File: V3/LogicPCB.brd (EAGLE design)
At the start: 171.9 x 151.6 mm, 58 parts, among them CON1 CUBE_ORANGE_, CON13 CON-6P-JST-XA, CON14 PINHEAD_1X04-2.54, CON15 CON-4P-JST-XA, CON17 CON-4P-JST-XA, CON18 CON-6P-JST-XA, CON19 USB-TYPE-C-VERT-PROD, CON2 CON-4P-JST-XA, CON20 PINHEAD_1X06-2.54, CON21 CON-4P-JST-XA, CON22 CON-4P-JST-XA, CON23 CON-4P-JST-XA, CON24 CON-4P-JST-XA, CON25 CON-4P-JST-XA, CON26 CON-4P-JST-XA, CON27 CON-4P-JST-XA, CON28 CON-4P-JST-XA, CON29 CON-4P-JST-XA, CON3 PINHEAD_1X08-2.54, CON30 CON-4P-JST-XA, CON32 CON-4P-JST-XA, CON35 CON-12P-JST-XA, CON4 CON-2P-JST-XA, CON5 CON-6P-JST-XA, CON6 CON-4P-JST-XA, CON7 PINHEAD_1X06-2.54, CON8 PINHEAD_1X08-2.54, IC2 AOZ1280, M1 05G_ETHERNET_SWITCH, Q1 IRLML0030

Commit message: updates for V3
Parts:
- removed CON3: PINHEAD_1X08-2.54, pinhead:1X08-PTH-2.54
- added CON9: PINHEAD_1X12-2.54, pinhead:1X12-PTH-2.54
- moved R2 3.47 mm to (-45.9, 56.5)
- moved SJ2 3.47 mm to (-48.2, 56.1)
- moved D10 3.16 mm to (-3.72, 53.8)
- moved R38 3.16 mm to (-7.10, 54.7)
- moved R37 3.16 mm to (-6.20, 56.3)
- moved CON30 2.24 mm to (26.4, 25.2)
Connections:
- net CAM_RX+ renamed ETH3_TX+
- net CAM_TX+ renamed ETH3_RX+
- net CAM_TX- renamed ETH3_RX-
- net CAN_RX- renamed ETH3_TX-
- net N$10 renamed ETH1_TX+
- net N$11 renamed ETH1_TX-
- net N$12 renamed ETH1_RX+
- net N$17 renamed ETH1_RX-
- net PL_ETH_RX+ renamed ETH5_TX-
- net PL_ETH_RX- renamed ETH5_TX+
- net PL_ETH_TX+ renamed ETH5_RX-
- net PL_ETH_TX- renamed ETH5_RX+
- net 5VFMU: now also CON9.6, CON9.7, CON9.8; no longer CON3.6, CON3.7, CON3.8
- net BATT_CURRENT: now also CON9.1; no longer CON3.1
- net BATT_VOLTAGE: now also CON9.2; no longer CON3.2
- net GND: now also CON35.10, CON9.11, CON9.12, CON9.3, CON9.4, CON9.5; no longer CON3.3, CON3.4, CON3.5
- net SERIAL3_RX: now also CON35.6; no longer CON35.8
- net SERIAL3_TX: now also CON35.5; no longer CON35.7
- net VDD_24V: now also CON35.7, CON35.8; no longer CON35.10
- net VDD_4V: now also CON9.10, CON9.9
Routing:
- net VDD_4V: track 31.3 -> 75.2 mm
- net CAN1_H: track 560.4 -> 547.7 mm
- net CAN1_L: track 565.9 -> 554.3 mm
- net M3PWM: track 83.7 -> 94.3 mm
- net M2PWM: track 88.3 -> 84.9 mm
- net N$23: track 9.40 -> 12.6 mm
- net SERIAL2_TX: track 47.5 -> 44.7 mm
- net SERIAL2_RX: track 45.2 -> 42.4 mm
- net 5VFMU: track 78.0 -> 75.2 mm
- net N$22: track 9.56 -> 12.3 mm
- net ETH3_TX+: track 94.2 -> 96.3 mm
- net ETH3_RX+: track 93.3 -> 95.4 mm
- net ETH3_TX-: track 93.5 -> 95.6 mm
- net ETH3_RX-: track 94.5 -> 96.6 mm
- net VDD_24V: track 57.6 -> 59.1 mm
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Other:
- board text added: "+"
- board text added: "CAN1 TERMINATION"
- board text added: "CTS"
- board text added: "CTS_4"
- board text added: "RX_4"
- board text added: "SER_RX"
- board text added: "SER_TX"
- board text added: "TX_4"
- board text removed: "ALT"
- board text removed: "B1H"
- board text removed: "B1L"
- board text removed: "B2H"
- board text removed: "B2L"
- board text removed: "B3H"
- board text removed: "B3L"
- board text removed: "BEACON"
- board text removed: "BTN"
- board text removed: "CAM"
- board text removed: "CAN1"
- board text removed: "CAN2"
- board text removed: "CR123A battery"
- board text removed: "DATA"
- board text removed: "DATA LINK"
- board text removed: "I2C"
- board text removed: "M1"
- board text removed: "M2"
- board text removed: "M4"
- board text removed: "M5"
- board text removed: "M6"
- board text removed: "PAYLOAD"
- board text removed: "PWRBTN"
- board text removed: "RES1"
- board text removed: "RX1"
- board text removed: "RX2"
- board text removed: "TELEM SBUS"
- board text removed: "TX1"
- board text removed: "TX2"

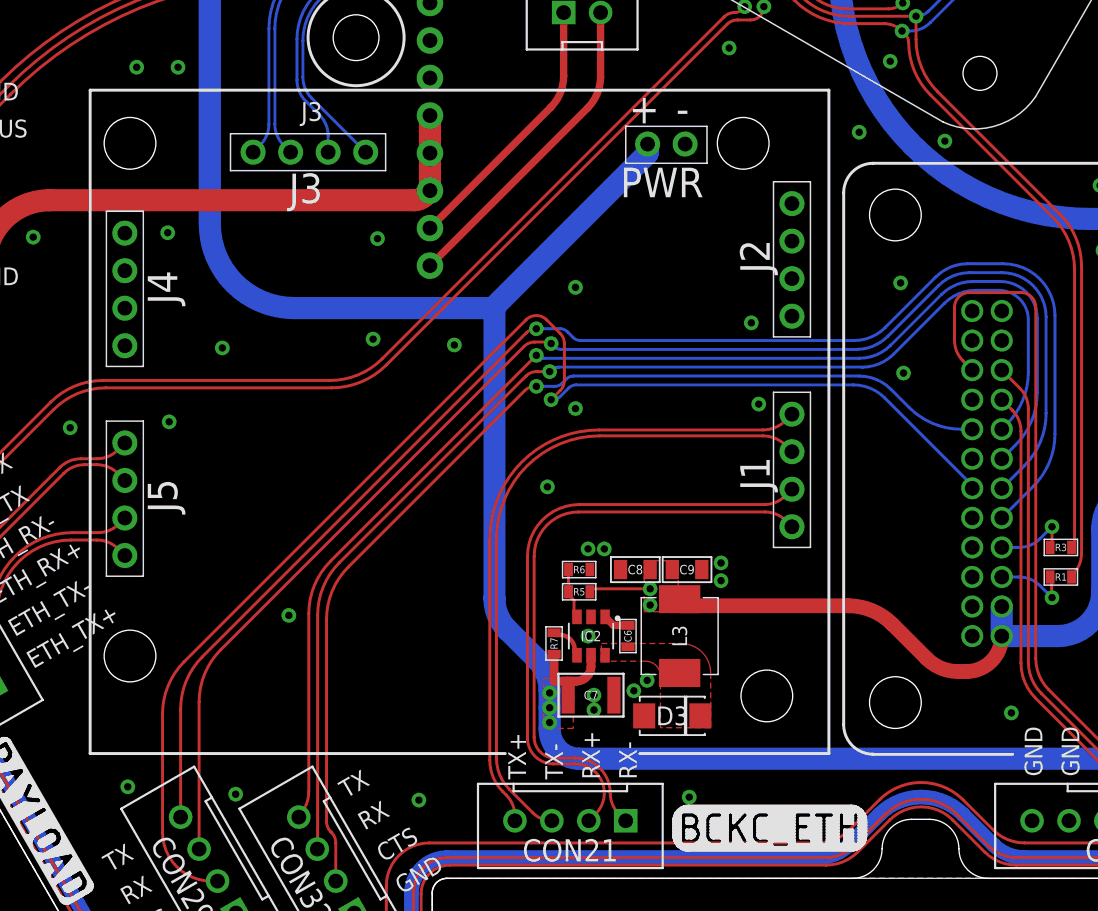
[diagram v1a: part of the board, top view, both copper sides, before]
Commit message: silkscreen updates
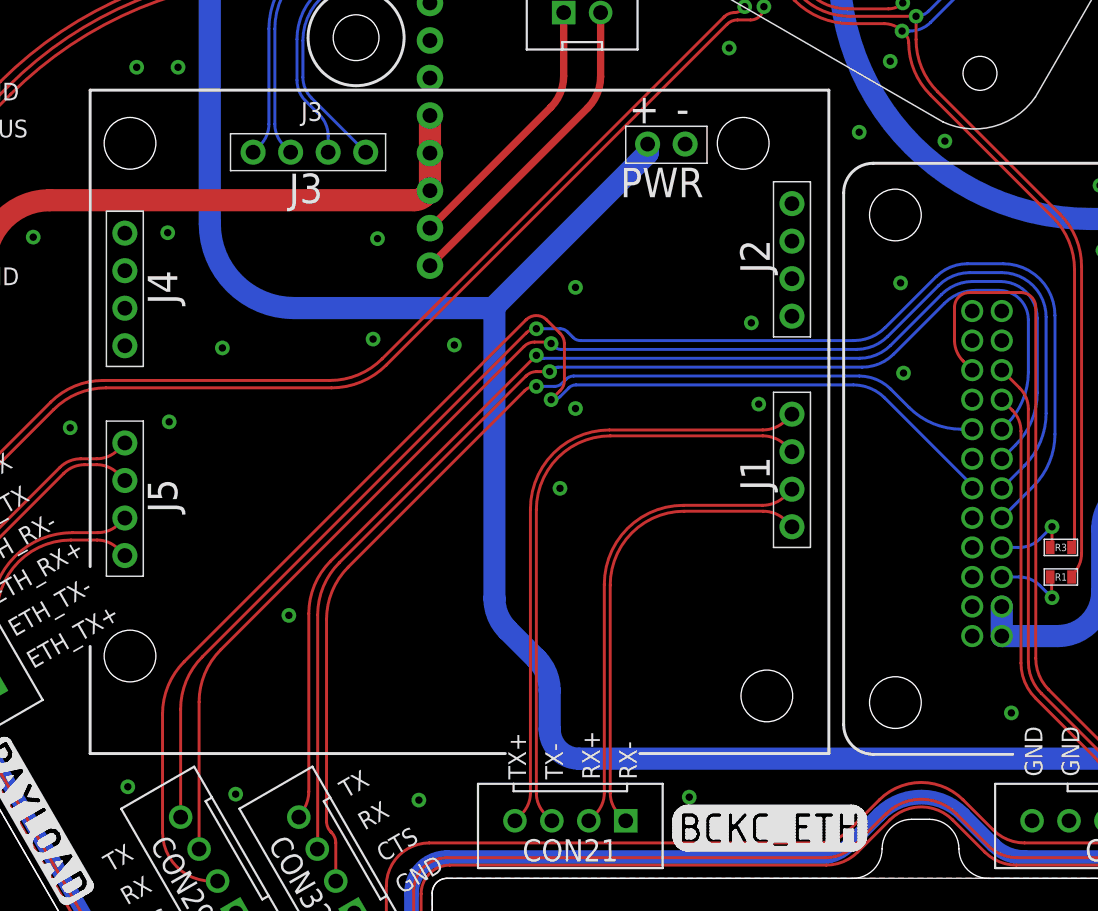
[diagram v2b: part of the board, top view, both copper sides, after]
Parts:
- removed C6: 22nF, rc:C0603
- removed C7: 10uF, rc:C1210
- removed C8, C9: 22uF, rc:C0805
- removed D3: SS34, Diodes:DO-214AC(SMA)
- removed IC2: AOZ1280, dc-dc:SOT23-6
- removed L3: 3.3uH, power_inductors:IHLP-2020BZ-01
- removed R5, R6: ???, rc:R0603
- removed R7: 51K, rc:R0603
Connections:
- removed net N$14: C6.2, IC2.1
- removed net N$15: IC2.3, R5.1, R6.1
- removed net N$16: IC2.4, R7.1
- removed net SW2: C6.1, D3.C, IC2.6, L3.P$1
- net GND: no longer C7.1, C8.1, C9.1, D3.A, IC2.2, R6.2
- net VDD_12V: no longer C7.2, IC2.5, R7.2
- net VDD_4V: no longer C8.2, C9.2, L3.P$2, R5.2
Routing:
- net VDD_4V: track 75.2 -> 45.9 mm, vias 2 -> 0
- net ETH1_RX+: track 40.9 -> 31.5 mm
- net ETH1_RX-: track 40.1 -> 30.9 mm
- net VDD_12V: track 270.8 -> 264.1 mm, vias 3 -> 0
- net N$15: track 3.44 -> 0.00 mm
- net ETH1_TX-: track 43.9 -> 41.0 mm
- net N$16: track 2.34 -> 0.00 mm
- net N$14: track 1.79 -> 0.00 mm
- net ETH1_TX+: track 43.3 -> 41.6 mm
- net GND: vias 113 -> 104
- removed copper zone on layer 1, net SW2
- removed copper zone on layer 1, net VDD_12V
- removed copper zone on layer 1, net VDD_4V

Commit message: V3 finalization
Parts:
- added C4: 10u, rc:C1206
- added C56: 10n, rc:C0603
- added C8: 47u, rc:C1206
- added CON11: CON-4P-JST-XA, Connectors:B04B-XASK-1
- added CON3: PINHEAD_1X04-2.54, pinhead:1X04-PTH-2.54
- added D11: SS34, Diodes:DO-214AC(SMA)
- added IC5: AOZ1280, dc-dc:SOT23-6
- added L1: 3.3uH, power_inductors:IHLP-2020BZ-01
- added M2: 05G_ETHERNET_SWITCH, ali_modules:05G_ETH_SWITCH
- added MODULE2: HLK-7688A, ali_modules:HLK-7688A
- added R30, R32: 51K, rc:R0603
- added R31: 16K, rc:R0603
- added T1, T2, T3, T4: H1102NL, misc:H1102
- moved R22 0.67 mm to (26.3, 52.7)
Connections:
- new net CAM_RX+: T1.9
- new net CAM_TX+: T1.14
- new net CAM_TX-: T1.16
- new net CAN_RX-: T1.11
- new net HLK_RX0: MODULE2.32
- new net HLK_RX1: MODULE2.16
- new net HLK_TX0: MODULE2.31
- new net HLK_TX1: MODULE2.15
- new net LINK0: MODULE2.13
- new net LINK1: MODULE2.12
- new net LINK2: MODULE2.11
- new net LINK4: MODULE2.9
- new net LINK_RX+: T4.9
- new net LINK_RX-: T4.11
- new net LINK_TX+: T4.14
- new net LINK_TX-: T4.16
- new net N$88: C56.2, IC5.1
- new net N$90: IC5.3, R30.1, R31.1
- new net N$91: IC5.4, R32.1
- new net P0_RX+: MODULE2.34, T2.3
- new net P0_RX-: MODULE2.35, T2.1
- new net P0_TX+: MODULE2.36, T2.8
- new net P0_TX-: MODULE2.37, T2.6
- new net P1_RX+: MODULE2.40, T1.8
- new net P1_RX-: MODULE2.41, T1.6
- new net P1_TX+: MODULE2.38, T1.3
- new net P1_TX-: MODULE2.39, T1.1
- new net P2_RX+: MODULE2.42, T4.8
- new net P2_RX-: MODULE2.43, T4.6
- new net P2_TX+: MODULE2.44, T4.3
- new net P2_TX-: MODULE2.45, T4.1
- new net P4_RX+: MODULE2.50, T3.8
- new net P4_RX-: MODULE2.51, T3.6
- new net P4_TX+: MODULE2.52, T3.3
- new net P4_TX-: MODULE2.53, T3.1
- new net PL_ETH_RX+: T3.11
- new net PL_ETH_RX-: T3.9
- new net PL_ETH_TX+: T3.16
- new net PL_ETH_TX-: T3.14
- new net SW: C56.1, D11.C, IC5.6, L1.P$1
- new net USB_DM: CON3.4, MODULE2.55
- new net USB_DP: CON3.3, MODULE2.54
- new net VDD_3V3: C8.P$1, L1.P$2, MODULE2.2, MODULE2.3, R30.2
- net GND: now also C4.P$1, C8.P$2, CON11.1, CON3.1, D11.A, IC5.2, MODULE2.1, MODULE2.21, MODULE2.23, MODULE2.4, MODULE2.56, MODULE2.P$1, MODULE2.P$2, MODULE2.P$3, R31.2
- net SERIAL4_RX: now also CON11.4; no longer CON30.4
- net SERIAL4_TX: now also CON11.3; no longer CON30.3
- net SERIAL5_RX: now also CON30.4
- net SERIAL5_TX: now also CON30.3
- net VDD_12V: now also C4.P$2, CON3.2, IC5.5, R32.2
- net VDD_5V: now also CON11.2
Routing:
- net SERIAL5_RX: track 0.00 -> 23.4 mm, vias 0 -> 1
- net SERIAL5_TX: track 0.00 -> 22.9 mm, vias 0 -> 1
- net VDD_5V: track 663.7 -> 679.2 mm
- net BATT_CURRENT: track 45.7 -> 54.9 mm
- net VDD_12V: track 264.1 -> 255.0 mm
- net BATT_VOLTAGE: track 50.2 -> 57.1 mm
- net ETH1_TX-: track 41.0 -> 35.8 mm
- net ETH1_TX+: track 41.6 -> 36.4 mm
- net ETH1_RX-: track 30.9 -> 29.2 mm
- net ETH1_RX+: track 31.5 -> 29.8 mm
- net SERIAL3_TX: track 106.1 -> 104.4 mm
- net SERIAL2_RX: track 42.4 -> 43.9 mm
- net ALARM: track 32.5 -> 33.9 mm
- net SERIAL2_TX: track 44.7 -> 46.0 mm
- net SERIAL4_TX: track 23.4 -> 24.4 mm, vias 2 -> 1
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
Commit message: V3 finished
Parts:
- removed C4: 10u, rc:C1206
- removed C56: 10n, rc:C0603
- removed C8: 47u, rc:C1206
- removed CON3: PINHEAD_1X04-2.54, pinhead:1X04-PTH-2.54
- removed D11: SS34, Diodes:DO-214AC(SMA)
- removed IC5: AOZ1280, dc-dc:SOT23-6
- removed L1: 3.3uH, power_inductors:IHLP-2020BZ-01
- removed M2: 05G_ETHERNET_SWITCH, ali_modules:05G_ETH_SWITCH
- removed MODULE2: HLK-7688A, ali_modules:HLK-7688A
- removed R30, R32: 51K, rc:R0603
- removed R31: 16K, rc:R0603
- removed T1, T2, T3, T4: H1102NL, misc:H1102
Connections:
- removed net CAM_RX+: T1.9
- removed net CAM_TX+: T1.14
- removed net CAM_TX-: T1.16
- removed net CAN_RX-: T1.11
- removed net HLK_RX0: MODULE2.32
- removed net HLK_RX1: MODULE2.16
- removed net HLK_TX0: MODULE2.31
- removed net HLK_TX1: MODULE2.15
- removed net LINK0: MODULE2.13
- removed net LINK1: MODULE2.12
- removed net LINK2: MODULE2.11
- removed net LINK4: MODULE2.9
- removed net LINK_RX+: T4.9
- removed net LINK_RX-: T4.11
- removed net LINK_TX+: T4.14
- removed net LINK_TX-: T4.16
- removed net N$88: C56.2, IC5.1
- removed net N$90: IC5.3, R30.1, R31.1
- removed net N$91: IC5.4, R32.1
- removed net P0_RX+: MODULE2.34, T2.3
- removed net P0_RX-: MODULE2.35, T2.1
- removed net P0_TX+: MODULE2.36, T2.8
- removed net P0_TX-: MODULE2.37, T2.6
- removed net P1_RX+: MODULE2.40, T1.8
- removed net P1_RX-: MODULE2.41, T1.6
- removed net P1_TX+: MODULE2.38, T1.3
- removed net P1_TX-: MODULE2.39, T1.1
- removed net P2_RX+: MODULE2.42, T4.8
- removed net P2_RX-: MODULE2.43, T4.6
- removed net P2_TX+: MODULE2.44, T4.3
- removed net P2_TX-: MODULE2.45, T4.1
- removed net P4_RX+: MODULE2.50, T3.8
- removed net P4_RX-: MODULE2.51, T3.6
- removed net P4_TX+: MODULE2.52, T3.3
- removed net P4_TX-: MODULE2.53, T3.1
- removed net PL_ETH_RX+: T3.11
- removed net PL_ETH_RX-: T3.9
- removed net PL_ETH_TX+: T3.16
- removed net PL_ETH_TX-: T3.14
- removed net SW: C56.1, D11.C, IC5.6, L1.P$1
- removed net USB_DM: CON3.4, MODULE2.55
- removed net USB_DP: CON3.3, MODULE2.54
- removed net VDD_3V3: C8.P$1, L1.P$2, MODULE2.2, MODULE2.3, R30.2
- net GND: no longer C4.P$1, C8.P$2, CON3.1, D11.A, IC5.2, MODULE2.1, MODULE2.21, MODULE2.23, MODULE2.4, MODULE2.56, MODULE2.P$1, MODULE2.P$2, MODULE2.P$3, R31.2
- net VDD_12V: no longer C4.P$2, CON3.2, IC5.5, R32.2
